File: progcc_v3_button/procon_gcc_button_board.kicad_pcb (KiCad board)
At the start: 2 copper layers, 110 x 54.3 mm, 31 parts, among them J1 Button Board, J2 bumpers, SW1 procon_abxy, SW2 procon_dpad, SW3 TL3315NF100Q, SW4 TL3315NF100Q, SW5 TL3315NF100Q, SW6 TL3315NF100Q

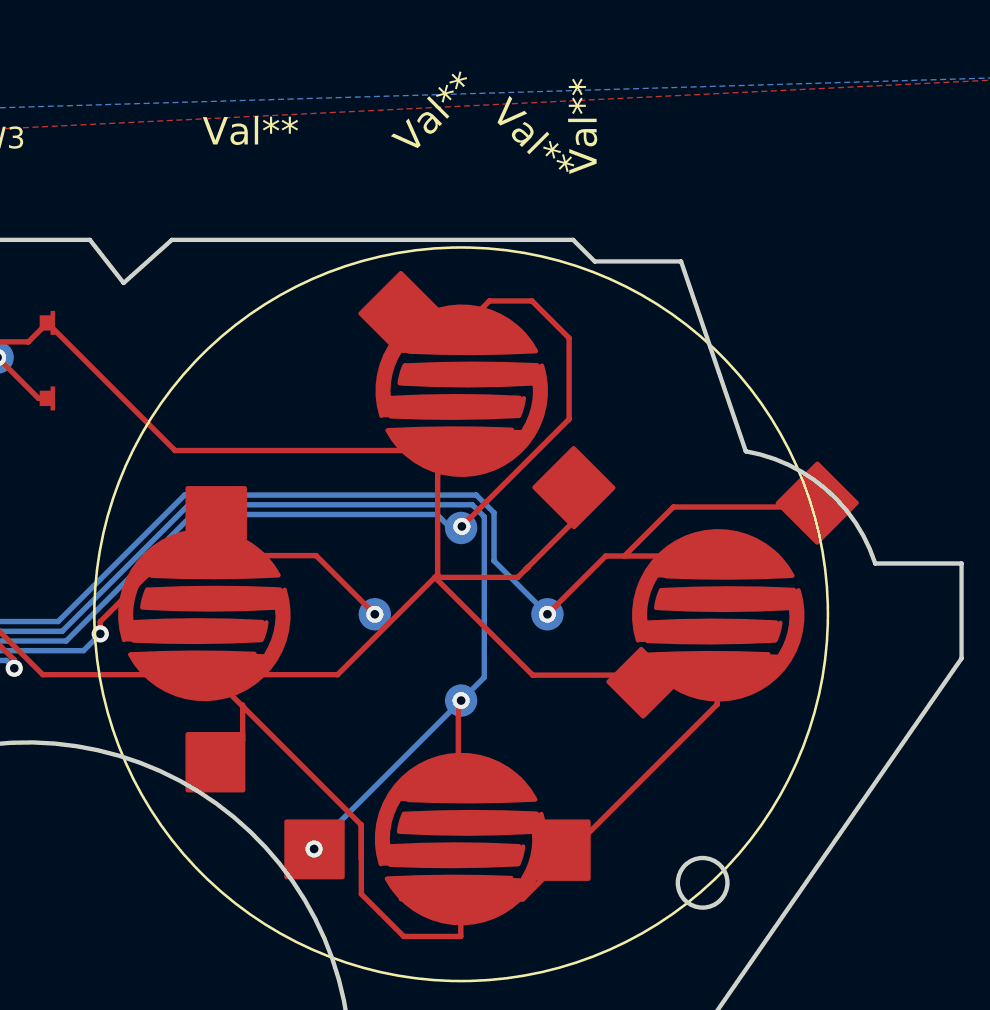
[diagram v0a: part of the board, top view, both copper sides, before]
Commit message: Update naming schema
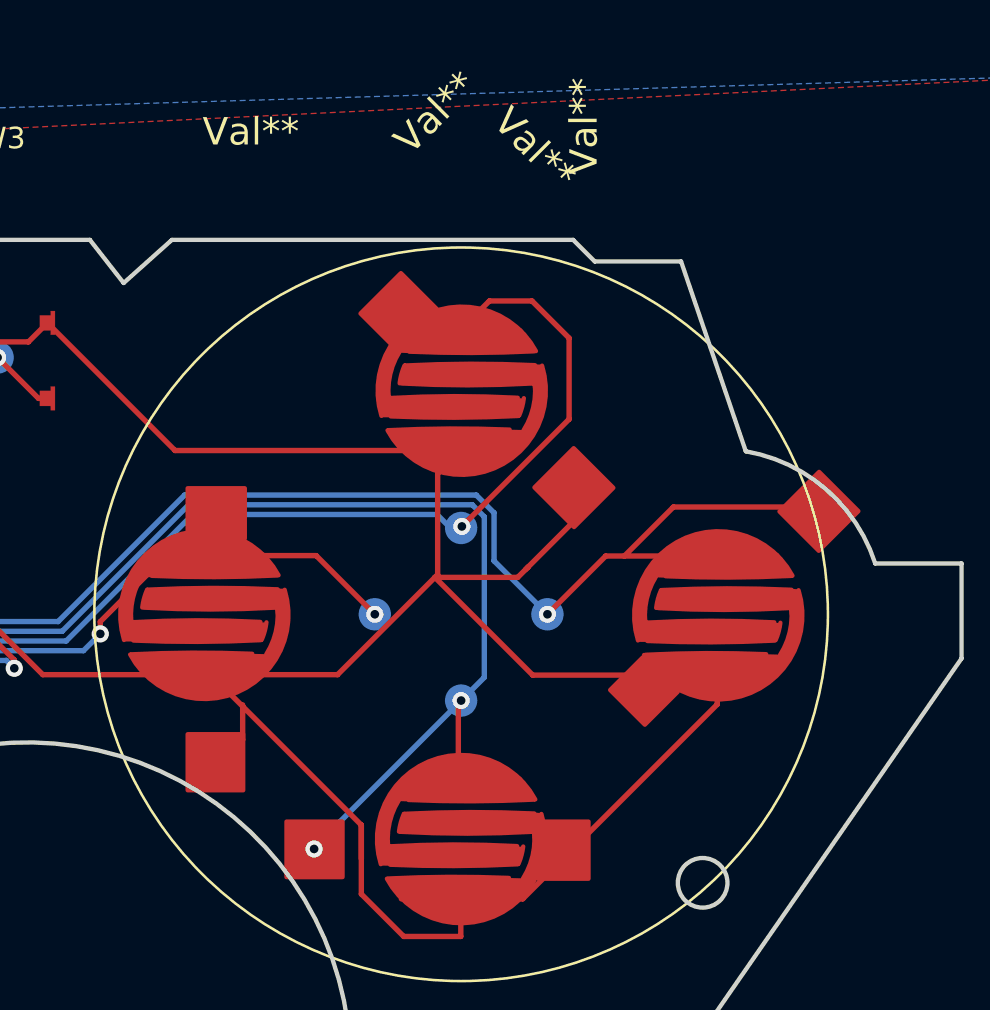
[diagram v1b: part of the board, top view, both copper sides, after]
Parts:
- moved Ref** 0.39 mm to (178.1, 45.1)
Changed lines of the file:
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@@
       (options (clearance outline) (anchor circle))
       (primitives
-    (gr_arc (start -0.922404 3.500009) (mid -0.999257 0.596666) (end -0.939258 -2.307074) (width 0.2))
-    (gr_arc (start -3.088552 -3.254467) (mid -1.977308 -3.182785) (end -0.948823 -2.755913) (width 0.2))
-    (gr_arc (start -3.920226 2.752478) (mid -4.000821 -0.204554) (end -3.93945 -3.162047) (width 0.2))
-    (gr_arc (start -3.08652 -3.209513) (mid -2.9983 -0.194752) (end -3.078506 2.820232) (width 0.2))
-    (gr_arc (start -3.091754 3.008173) (mid -3.501417 2.929165) (end -3.895504 2.792192) (width 0.2))
+    (gr_arc (start -0.922404 3.500009) (mid -0.999257 0.596677) (end -0.939259 -2.307053) (width 0.2))
+    (gr_arc (start -3.088552 -3.254467) (mid -1.977311 -3.182786) (end -0.948828 -2.755916) (width 0.2))
+    (gr_arc (start -3.920226 2.752478) (mid -4.000821 -0.204549) (end -3.939451 -3.162037) (width 0.2))
+    (gr_arc (start -3.08652 -3.209513) (mid -2.998383 -0.241884) (end -3.073451 2.726105) (width 0.2))
+    (gr_arc (start -3.091754 3.008173) (mid -3.49898 2.929819) (end -3.890867 2.794183) (width 0.2))
         (gr_poly (pts
             (xy -3.91 2.75)
@@
       (options (clearance outline) (anchor circle))
       (primitives
-    (gr_arc (start -0.922404 3.500009) (mid -0.999257 0.596666) (end -0.939258 -2.307074) (width 0.2))
-    (gr_arc (start -3.088552 -3.254467) (mid -1.977308 -3.182785) (end -0.948823 -2.755913) (width 0.2))
-    (gr_arc (start -3.920226 2.752478) (mid -4.000821 -0.204554) (end -3.93945 -3.162047) (width 0.2))
-    (gr_arc (start -3.08652 -3.209513) (mid -2.9983 -0.194752) (end -3.078506 2.820232) (width 0.2))
-    (gr_arc (start -3.091754 3.008173) (mid -3.501417 2.929165) (end -3.895504 2.792192) (width 0.2))
+    (gr_arc (start -0.922404 3.500009) (mid -0.999257 0.596677) (end -0.939259 -2.307053) (width 0.2))
+    (gr_arc (start -3.088552 -3.254467) (mid -1.977311 -3.182786) (end -0.948828 -2.755916) (width 0.2))
+    (gr_arc (start -3.920226 2.752478) (mid -4.000821 -0.204549) (end -3.939451 -3.162037) (width 0.2))
+    (gr_arc (start -3.08652 -3.209513) (mid -2.998383 -0.241884) (end -3.073451 2.726105) (width 0.2))
+    (gr_arc (start -3.091754 3.008173) (mid -3.49898 2.929819) (end -3.890867 2.794183) (width 0.2))
         (gr_poly (pts
             (xy -3.91 2.75)
@@
       (options (clearance outline) (anchor circle))
       (primitives
-    (gr_arc (start -0.922404 3.500009) (mid -0.999257 0.596666) (end -0.939258 -2.307074) (width 0.2))
-    (gr_arc (start -3.088552 -3.254467) (mid -1.977308 -3.182785) (end -0.948823 -2.755913) (width 0.2))
-    (gr_arc (start -3.920226 2.752478) (mid -4.000821 -0.204554) (end -3.93945 -3.162047) (width 0.2))
-    (gr_arc (start -3.08652 -3.209513) (mid -2.9983 -0.194752) (end -3.078506 2.820232) (width 0.2))
-    (gr_arc (start -3.091754 3.008173) (mid -3.501417 2.929165) (end -3.895504 2.792192) (width 0.2))
+    (gr_arc (start -0.922404 3.500009) (mid -0.999257 0.596677) (end -0.939259 -2.307053) (width 0.2))
+    (gr_arc (start -3.088552 -3.254467) (mid -1.977311 -3.182786) (end -0.948828 -2.755916) (width 0.2))
+    (gr_arc (start -3.920226 2.752478) (mid -4.000821 -0.204549) (end -3.939451 -3.162037) (width 0.2))
+    (gr_arc (start -3.08652 -3.209513) (mid -2.998383 -0.241884) (end -3.073451 2.726105) (width 0.2))
+    (gr_arc (start -3.091754 3.008173) (mid -3.49898 2.929819) (end -3.890867 2.794183) (width 0.2))
         (gr_poly (pts
             (xy -3.91 2.75)
@@
       (options (clearance outline) (anchor circle))
       (primitives
-    (gr_arc (start -0.922404 3.500009) (mid -0.999257 0.596666) (end -0.939258 -2.307074) (width 0.2))
-    (gr_arc (start -3.088552 -3.254467) (mid -1.977308 -3.182785) (end -0.948823 -2.755913) (width 0.2))
-    (gr_arc (start -3.920226 2.752478) (mid -4.000821 -0.204554) (end -3.93945 -3.162047) (width 0.2))
-    (gr_arc (start -3.08652 -3.209513) (mid -2.9983 -0.194752) (end -3.078506 2.820232) (width 0.2))
-    (gr_arc (start -3.091754 3.008173) (mid -3.501417 2.929165) (end -3.895504 2.792192) (width 0.2))
+    (gr_arc (start -0.922404 3.500009) (mid -0.999257 0.596677) (end -0.939259 -2.307053) (width 0.2))
+    (gr_arc (start -3.088552 -3.254467) (mid -1.977311 -3.182786) (end -0.948828 -2.755916) (width 0.2))
+    (gr_arc (start -3.920226 2.752478) (mid -4.000821 -0.204549) (end -3.939451 -3.162037) (width 0.2))
+    (gr_arc (start -3.08652 -3.209513) (mid -2.998383 -0.241884) (end -3.073451 2.726105) (width 0.2))
+    (gr_arc (start -3.091754 3.008173) (mid -3.49898 2.929819) (end -3.890867 2.794183) (width 0.2))
         (gr_poly (pts
             (xy -3.91 2.75)
@@
       (options (clearance outline) (anchor circle))
       (primitives
-    (gr_arc (start 3.94255 -2.57544) (mid 4.023401 0.489162) (end 3.951776 3.553993) (width 0.2))
+    (gr_arc (start 3.94255 -2.57544) (mid 4.023297 0.435377) (end 3.956869 3.446544) (width 0.2))
     (gr_arc (start 3.110877 3.431506) (mid 1.982318 3.355744) (end 0.941064 2.913959) (width 0.2))
         (gr_poly (pts
@@
     (gr_arc (start 3.936518 3.770339) (mid -0.825787 1.555821) (end 0.935049 -3.392219) (width 0.2))
     (gr_arc (start 3.108844 3.38655) (mid 3.020582 0.324645) (end 3.10605 -2.737339) (width 0.2))
-    (gr_arc (start 0.944728 -3.32297) (mid 1.0214 -0.473391) (end 0.966241 2.376685) (width 0.2))
+    (gr_arc (start 0.944728 -3.32297) (mid 1.021174 -0.52717) (end 0.970715 2.26922) (width 0.2))
       ))
     (pad "GND" smd custom locked (at -11.95 2.8 90) (size 1.524 1.524) (layers "F.Cu" "F.Paste" "F.Mask")
@@
       (options (clearance outline) (anchor circle))
       (primitives
-    (gr_arc (start 3.94255 -2.57544) (mid 4.023401 0.489162) (end 3.951776 3.553993) (width 0.2))
+    (gr_arc (start 3.94255 -2.57544) (mid 4.023297 0.435377) (end 3.956869 3.446544) (width 0.2))
     (gr_arc (start 3.110877 3.431506) (mid 1.982318 3.355744) (end 0.941064 2.913959) (width 0.2))
         (gr_poly (pts
@@
     (gr_arc (start 3.936518 3.770339) (mid -0.825787 1.555821) (end 0.935049 -3.392219) (width 0.2))
     (gr_arc (start 3.108844 3.38655) (mid 3.020582 0.324645) (end 3.10605 -2.737339) (width 0.2))
-    (gr_arc (start 0.944728 -3.32297) (mid 1.0214 -0.473391) (end 0.966241 2.376685) (width 0.2))
+    (gr_arc (start 0.944728 -3.32297) (mid 1.021174 -0.52717) (end 0.970715 2.26922) (width 0.2))
       ))
     (pad "GND" smd custom locked (at -0.05 13.19 90) (size 1.524 1.524) (layers "F.Cu" "F.Paste" "F.Mask")
@@
       (options (clearance outline) (anchor circle))
       (primitives
-    (gr_arc (start 3.94255 -2.57544) (mid 4.023401 0.489162) (end 3.951776 3.553993) (width 0.2))
+    (gr_arc (start 3.94255 -2.57544) (mid 4.023297 0.435377) (end 3.956869 3.446544) (width 0.2))
     (gr_arc (start 3.110877 3.431506) (mid 1.982318 3.355744) (end 0.941064 2.913959) (width 0.2))
         (gr_poly (pts
@@
     (gr_arc (start 3.936518 3.770339) (mid -0.825787 1.555821) (end 0.935049 -3.392219) (width 0.2))
     (gr_arc (start 3.108844 3.38655) (mid 3.020582 0.324645) (end 3.10605 -2.737339) (width 0.2))
-    (gr_arc (start 0.944728 -3.32297) (mid 1.0214 -0.473391) (end 0.966241 2.376685) (width 0.2))
+    (gr_arc (start 0.944728 -3.32297) (mid 1.021174 -0.52717) (end 0.970715 2.26922) (width 0.2))
       ))
     (pad "GND" smd custom locked (at -0.02 -7.59 90) (size 1.524 1.524) (layers "F.Cu" "F.Paste" "F.Mask")
@@
       (options (clearance outline) (anchor circle))
       (primitives
-    (gr_arc (start 3.94255 -2.57544) (mid 4.023401 0.489162) (end 3.951776 3.553993) (width 0.2))
+    (gr_arc (start 3.94255 -2.57544) (mid 4.023297 0.435377) (end 3.956869 3.446544) (width 0.2))
     (gr_arc (start 3.110877 3.431506) (mid 1.982318 3.355744) (end 0.941064 2.913959) (width 0.2))
         (gr_poly (pts
@@
     (gr_arc (start 3.936518 3.770339) (mid -0.825787 1.555821) (end 0.935049 -3.392219) (width 0.2))
     (gr_arc (start 3.108844 3.38655) (mid 3.020582 0.324645) (end 3.10605 -2.737339) (width 0.2))
-    (gr_arc (start 0.944728 -3.32297) (mid 1.0214 -0.473391) (end 0.966241 2.376685) (width 0.2))
+    (gr_arc (start 0.944728 -3.32297) (mid 1.021174 -0.52717) (end 0.970715 2.26922) (width 0.2))
       ))
   )
@@
   )
   (footprint "procon_gcc:ABXY_Contact_Omron_Switch" (layer "F.Cu")
-    (at 178.024 44.694 135)
+    (at 178.101636 45.07584 135)
     (attr through_hole)
     (fp_text reference "Ref**" (at -3.15 -6.5 135) (layer "F.SilkS") hide
@@
       (polygon
         (pts
-          (xy 174.323872 43.39614)
-          (xy 176.609786 41.017045)
-          (xy 179.296792 41.158466)
-          (xy 181.559534 43.421208)
-          (xy 181.700955 46.108214)
-          (xy 179.438214 48.370955)
-          (xy 176.751208 48.229534)
-          (xy 174.488466 45.966792)
+          (xy 174.401508 43.77798)
+          (xy 176.687422 41.398885)
+          (xy 179.374428 41.540306)
+          (xy 181.63717 43.803048)
+          (xy 181.778591 46.490054)
+          (xy 179.51585 48.752795)
+          (xy 176.828844 48.611374)
+          (xy 174.566102 46.348632)
         )
       )
